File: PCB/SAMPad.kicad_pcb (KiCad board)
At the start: 2 copper layers, 73.2 x 116 mm, 162 parts, among them P1 USB_CONN, P1_2 USB_CONN, P4 CONN_6, P5 CONN_6, P6 ISP6, U1 ATMEGA32U4, U3 IP4234CZ6, U4 AP3417C, U5 PAM2804, X1 CRYSTAL

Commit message: v0.3
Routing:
- net VSS: track 537.2 -> 487.0 mm
- net /mcu/ROW6: track 137.2 -> 134.4 mm, vias 2 -> 4
- net 3V3: track 491.5 -> 494.1 mm

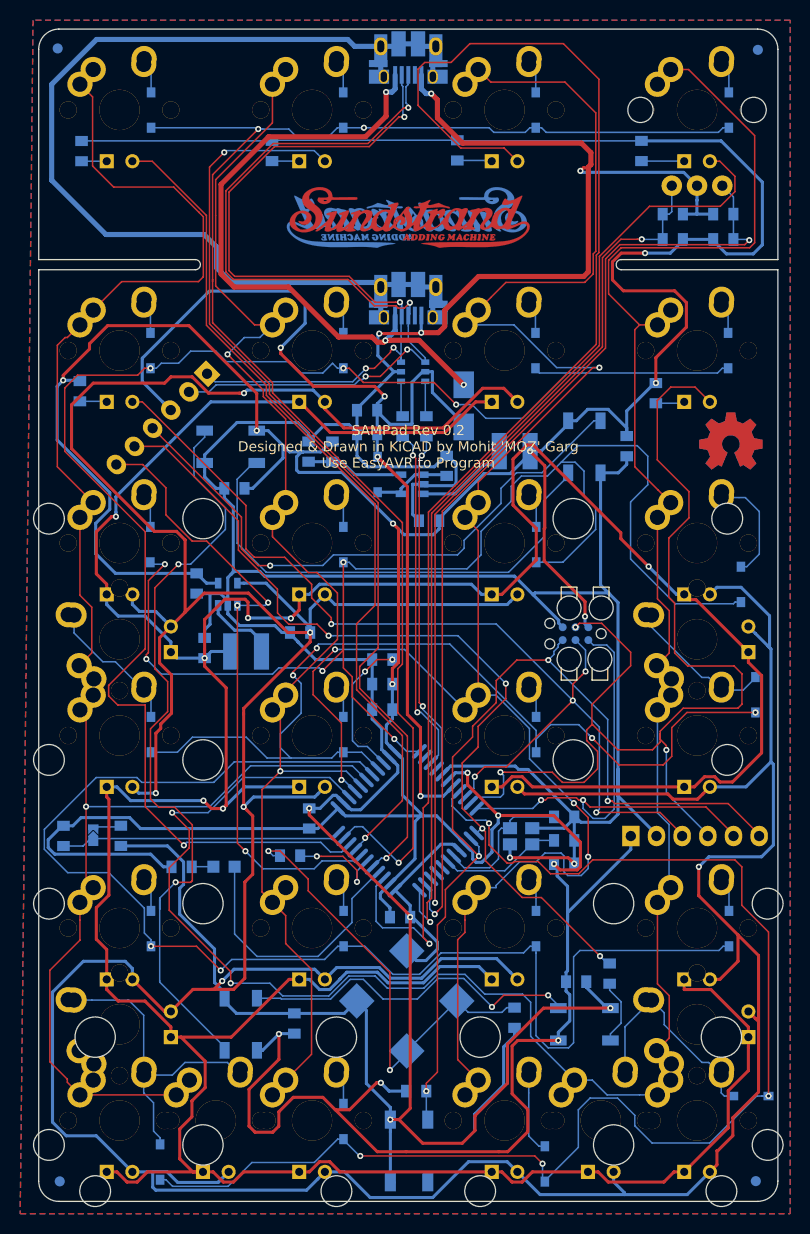
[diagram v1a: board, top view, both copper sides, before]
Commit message: Rev 0.4 - Removed 3.3V regulator
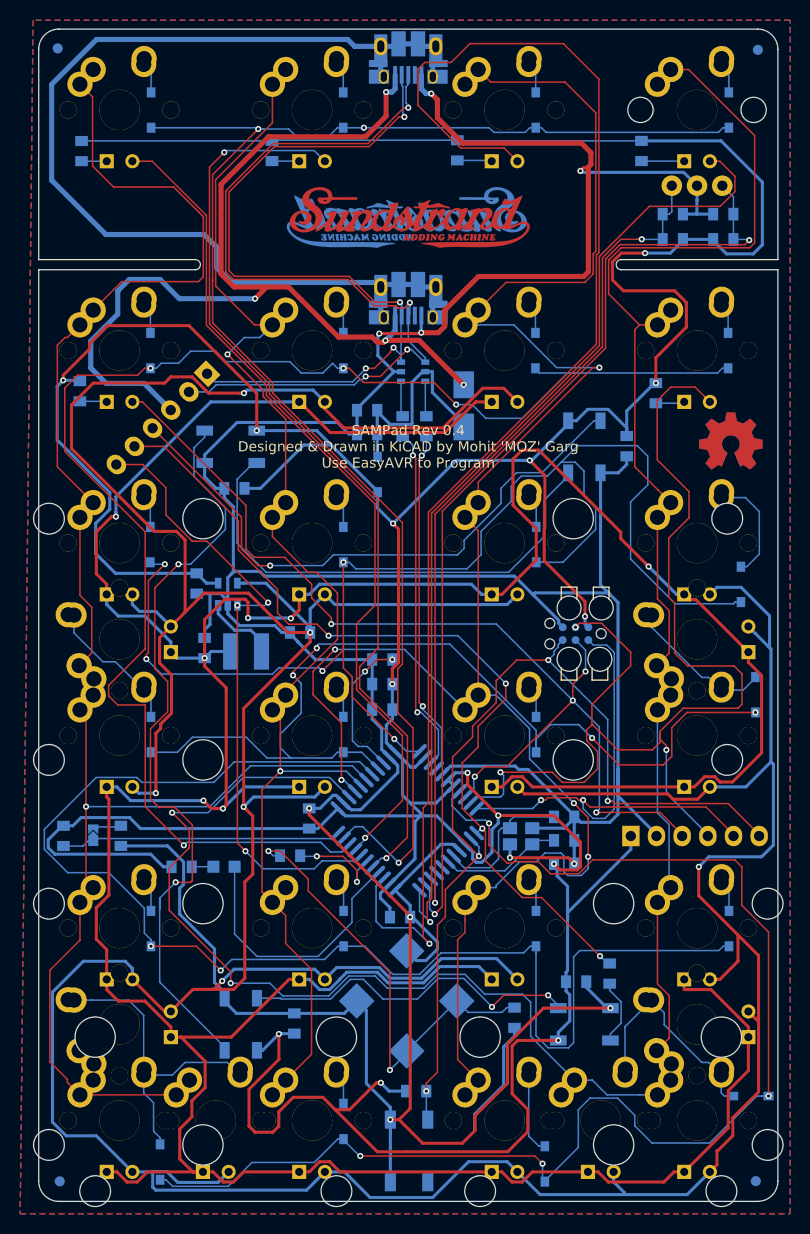
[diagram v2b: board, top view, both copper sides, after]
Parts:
- removed C15: 4.7uF, prettylib:SMD_0805
- removed C16: 10uF, prettylib:SMD_0805
- removed L1: 2.2uH, prettylib:Inductor_Bourn_4mmx4mm
- removed R7: 453k, prettylib:SMD_0805
- removed R8: 100k, prettylib:SMD_0805
- removed U4: AP3417C, prettylib:SOT-23-5
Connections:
- C1 pad 1: /mcu/VUSB -> Net-(C1-Pad1)
- C17 pad 1: 3V3 -> +5V
- C2 pad 1: 3V3 -> +5V
- C3 pad 1: 3V3 -> +5V
- C4 pad 1: 3V3 -> +5V
- C6 pad 1: 3V3 -> +5V
- C7 pad 1: 3V3 -> +5V
- C9 pad 1: /mcu/VUSB -> Net-(C1-Pad1)
- CLED1 pad 2: 3V3 -> +5V
- CLED2 pad 2: 3V3 -> +5V
- CLED3 pad 1: 3V3 -> +5V
- CLED4 pad 1: 3V3 -> +5V
- D1 pad 1: /mcu/VUSB -> Net-(C1-Pad1)
- D1 pad 2: /mcu/VINU -> +5V
- F1 pad 1: Net-(F1-Pad1) -> /mcu/VUSB
- F1 pad 2: /mcu/VUSB -> Net-(C1-Pad1)
- LEDG1 pad 1: 3V3 -> +5V
- LEDG2 pad 1: 3V3 -> +5V
- LEDG3 pad 1: 3V3 -> +5V
- LEDG4 pad 1: 3V3 -> +5V
- P1 pad 1: Net-(F1-Pad1) -> /mcu/VUSB
- P1_2 pad 1: Net-(F1-Pad1) -> /mcu/VUSB
- P5 pad 1: 3V3 -> +5V
- P6 pad 2: 3V3 -> +5V
- R14 pad 2: 3V3 -> +5V
- R34 pad 2: 3V3 -> +5V
- R35 pad 1: 3V3 -> +5V
- R9 pad 2: 3V3 -> +5V
- RI1 pad 2: 3V3 -> +5V
- RI2 pad 2: 3V3 -> +5V
- RI3 pad 2: 3V3 -> +5V
- RI4 pad 2: 3V3 -> +5V
- RI5 pad 2: 3V3 -> +5V
- RI6 pad 2: 3V3 -> +5V
- RI7 pad 2: 3V3 -> +5V
- U1 pad 14: 3V3 -> +5V
- U1 pad 2: (no net) -> +5V
- U1 pad 24: 3V3 -> +5V
- U1 pad 34: 3V3 -> +5V
- U1 pad 44: 3V3 -> +5V
- U1 pad 6: 3V3 -> +5V
- U1 pad 7: /mcu/VUSB -> +5V
- U3 pad 5: /mcu/VUSB -> Net-(C1-Pad1)
- U5 pad 4: 3V3 -> +5V
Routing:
- net +5V: track 0.00 -> 501.0 mm, vias 0 -> 14
- net 3V3: track 494.1 -> 0.00 mm, vias 14 -> 0
- net Net-(F1-Pad1): track 64.4 -> 0.00 mm, vias 3 -> 0
- net VSS: track 487.0 -> 461.3 mm
- net Net-(C1-Pad1): track 0.00 -> 22.1 mm
- net Net-(L1-Pad2): track 9.89 -> 0.00 mm
- net Net-(R7-Pad2): track 9.68 -> 0.00 mm
- net /mcu/VINU: track 8.04 -> 0.00 mm
- net /mcu/VUSB: track 106.5 -> 99.2 mm
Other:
- board text added: "SAMPad Rev 0.4 Designed & Drawin in KiCAD by Mohit 'MOZ' Garg Use EasyAVR to Program"
- board text added: "SAMPad Rev 0.4 Designed & Drawn in KiCAD by Mohit 'MOZ' Garg Use EasyAVR to Program"
- board text removed: "SAMPad Rev 0.2 Designed & Drawin in KiCAD by Mohit 'MOZ' Garg Use EasyAVR to Program"
- board text removed: "SAMPad Rev 0.2 Designed & Drawn in KiCAD by Mohit 'MOZ' Garg Use EasyAVR to Program"

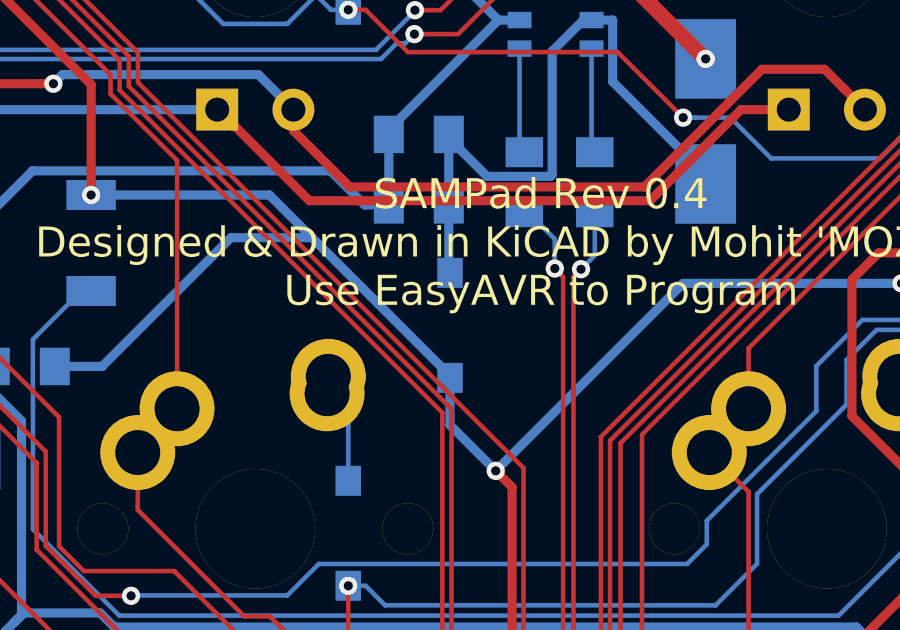
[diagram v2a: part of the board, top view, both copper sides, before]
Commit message: Removed Shottky diode
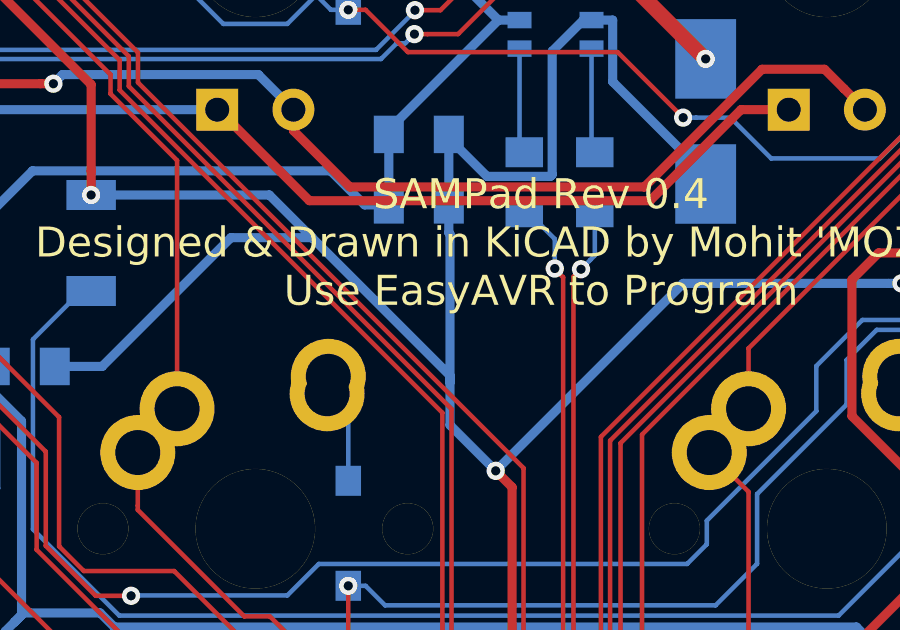
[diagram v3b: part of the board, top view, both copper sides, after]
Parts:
- removed D1: SCHOTTKY, prettylib:SOD123-DIODE
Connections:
- C1 pad 1: Net-(C1-Pad1) -> +5V
- C9 pad 1: Net-(C1-Pad1) -> +5V
- F1 pad 2: Net-(C1-Pad1) -> +5V
- U3 pad 5: Net-(C1-Pad1) -> +5V
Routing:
- net +5V: track 501.0 -> 526.7 mm
- net Net-(C1-Pad1): track 22.1 -> 0.00 mm
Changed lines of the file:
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@@
 (kicad_pcb (version 4) (host pcbnew 4.0.1-stable)
   (general
-    (links 366)
-    (no_connects 1)
+    (links 365)
+    (no_connects 0)
     (area 91.936499 68.123999 165.213501 184.263501)
     (thickness 1.6)
     (drawings 21)
-    (tracks 2026)
+    (tracks 2028)
     (zones 0)
-    (modules 156)
-    (nets 81)
+    (modules 155)
+    (nets 80)
   )
   (page A4)
@@
   )
   (setup
-    (last_trace_width 0.508)
+    (last_trace_width 0.1524)
     (user_trace_width 0.1524)
     (user_trace_width 0.2032)
@@
   (net 78 "Net-(BZ1-Pad1)")
   (net 79 +5V)
-  (net 80 "Net-(C1-Pad1)")
   (net_class Default "This is the default net class."
     (clearance 0.1524)
@@
     (add_net /mcu/XTAL2)
     (add_net "Net-(BZ1-Pad1)")
-    (add_net "Net-(C1-Pad1)")
     (add_net "Net-(C5-Pad1)")
     (add_net "Net-(D1:1-Pad1)")
@@
       (net 63 /mcu/D+))
     (pad 5 smd rect (at 0 1.2 90) (size 0.55 0.8) (layers B.Cu B.Paste B.Mask)
-      (net 80 "Net-(C1-Pad1)"))
+      (net 79 +5V))
     (pad 6 smd rect (at -0.95 1.2 90) (size 0.55 0.8) (layers B.Cu B.Paste B.Mask)
       (net 69 "Net-(R3-Pad1)"))
@@
       (net 2 /mcu/VUSB))
     (pad 2 smd rect (at 2.08534 0 180) (size 2.02946 2.65176) (layers B.Cu B.Paste B.Mask)
-      (net 80 "Net-(C1-Pad1)"))
+      (net 79 +5V))
   )
   (module prettylib:SOD123-DIODE (layer B.Cu)
@@
     )
   )
-  (module prettylib:SOD123-DIODE (layer B.Cu)
-    (at 125.5395 112.268)
-    (descr DIODE)
-    (tags DIODE)
-    (fp_text reference D1 (at -1.7145 0.127 270) (layer B.SilkS)
-      (effects (font (size 1.016 1.016) (thickness 0.2032)) (justify mirror))
-    )
-    (fp_text value SCHOTTKY (at 1.905 0 270) (layer B.SilkS) hide
-      (effects (font (size 1.016 1.016) (thickness 0.2032)) (justify mirror))
-    )
-    (fp_line (start -0.8509 0.70104) (end 0.8509 0.70104) (layer B.SilkS) (width 0.22098))
-    (fp_line (start -0.8509 1.45034) (end -0.59944 1.45034) (layer B.SilkS) (width 0.22098))
-    (fp_line (start 0.8509 1.45034) (end 0.59944 1.45034) (layer B.SilkS) (width 0.22098))
-    (fp_line (start 0.8509 -1.45034) (end 0.59944 -1.45034) (layer B.SilkS) (width 0.22098))
-    (fp_line (start -0.8509 -1.45034) (end -0.59944 -1.45034) (layer B.SilkS) (width 0.22098))
-    (fp_line (start -0.8509 -1.45034) (end -0.8509 1.45034) (layer B.SilkS) (width 0.22098))
-    (fp_line (start 0.8509 -1.45034) (end 0.8509 1.45034) (layer B.SilkS) (width 0.22098))
-    (pad 2 smd rect (at 0 1.7526 90) (size 1.00076 0.8509) (layers B.Cu B.Paste B.Mask)
-      (net 79 +5V))
-    (pad 1 smd rect (at 0 -1.74752 90) (size 1.00076 0.8509) (layers B.Cu B.Paste B.Mask)
-      (net 80 "Net-(C1-Pad1)"))
-    (model SOD123.wrl
-      (at (xyz 0 0 -0.003))
-      (scale (xyz 0.393701 0.393701 0.393701))
-      (rotate (xyz 0 0 90))
-    )
-  )
   (module prettylib:SMD_0805 (layer B.Cu)
     (at 150.1902 109.4613 270)
@@
     (fp_line (start 1.8 1) (end 1.8 -1) (layer B.SilkS) (width 0.15))
     (pad 1 smd rect (at -1 0 180) (size 1 1.25) (layers B.Cu B.Paste B.Mask)
-      (net 80 "Net-(C1-Pad1)"))
+      (net 79 +5V))
     (pad 2 smd rect (at 1 0 180) (size 1 1.25) (layers B.Cu B.Paste B.Mask)
       (net 1 VSS))
@@
     (fp_line (start 1.8 1) (end 1.8 -1) (layer B.SilkS) (width 0.15))
     (pad 1 smd rect (at -1 0 180) (size 1 1.25) (layers B.Cu B.Paste B.Mask)
-      (net 80 "Net-(C1-Pad1)"))
+      (net 79 +5V))
     (pad 2 smd rect (at 1 0 180) (size 1 1.25) (layers B.Cu B.Paste B.Mask)
       (net 1 VSS))
@@
   (segment (start 128.4224 169.313147) (end 129.376993 168.358554) (width 0.1524) (layer B.Cu) (net 78))
   (segment (start 129.376993 168.358554) (end 133.372147 164.3634) (width 0.1524) (layer B.Cu) (net 78))
+  (segment (start 125.5395 114.0206) (end 125.5395 114.173) (width 0.3048) (layer B.Cu) (net 79))
+  (segment (start 125.5395 114.173) (end 125.5395 115.5954) (width 0.3048) (layer B.Cu) (net 79))
+  (segment (start 125.5 108.2548) (end 125.5 109.1846) (width 0.3048) (layer B.Cu) (net 79))
+  (segment (start 125.5 109.1846) (end 125.5395 109.2241) (width 0.3048) (layer B.Cu) (net 79))
+  (segment (start 125.5395 109.2241) (end 125.5395 114.173) (width 0.3048) (layer B.Cu) (net 79))
   (segment (start 133.080071 143.057241) (end 133.040759 143.057241) (width 0.3048) (layer B.Cu) (net 79))
   (segment (start 133.040759 143.057241) (end 131.318 144.78) (width 0.3048) (layer B.Cu) (net 79))
@@
   (segment (start 144.4 106.948) (end 144.4 107.2735) (width 0.3048) (layer B.Cu) (net 79))
   (segment (start 140.157948 110.871) (end 140.589 110.871) (width 0.3048) (layer B.Cu) (net 79))
-  (segment (start 125.5395 114.0206) (end 125.5395 115.5954) (width 0.3048) (layer B.Cu) (net 79))
   (segment (start 125.5395 115.5954) (end 127.0635 117.1194) (width 0.3048) (layer B.Cu) (net 79))
   (segment (start 125.505454 179.2859) (end 121.352554 175.133) (width 0.3048) (layer F.Cu) (net 79))
@@
   (segment (start 151.6507 79.2513) (end 133.4897 79.2513) (width 0.1524) (layer B.Cu) (net 79))
   (segment (start 133.4897 79.2513) (end 133.4262 79.1878) (width 0.1524) (layer B.Cu) (net 79))
-  (segment (start 125.5 108.2548) (end 125.5 110.48098) (width 0.3048) (layer B.Cu) (net 80))
-  (segment (start 125.5 110.48098) (end 125.5395 110.52048) (width 0.3048) (layer B.Cu) (net 80))
-  (segment (start 125.5 105.9053) (end 125.5 108.2548) (width 0.3048) (layer B.Cu) (net 80))
-  (segment (start 130.2574 102.0953) (end 129.983758 102.0953) (width 0.3048) (layer B.Cu) (net 80))
-  (segment (start 128.945801 103.133257) (end 128.945801 107.243841) (width 0.3048) (layer B.Cu) (net 80))
-  (segment (start 129.983758 102.0953) (end 128.945801 103.133257) (width 0.3048) (layer B.Cu) (net 80))
-  (segment (start 128.945801 107.243841) (end 128.884841 107.304801) (width 0.3048) (layer B.Cu) (net 80))
-  (segment (start 128.884841 107.304801) (end 126.774501 107.304801) (width 0.3048) (layer B.Cu) (net 80))
-  (segment (start 126.774501 107.304801) (end 125.5 106.0303) (width 0.3048) (layer B.Cu) (net 80))
-  (segment (start 125.5 106.0303) (end 125.5 105.9053) (width 0.3048) (layer B.Cu) (net 80))
-  (segment (start 134.0612 107.55884) (end 134.0612 107.24769) (width 0.3048) (layer B.Cu) (net 80))
-  (segment (start 134.0612 107.24769) (end 130.962201 104.148691) (width 0.3048) (layer B.Cu) (net 80))
-  (segment (start 130.962201 104.148691) (end 130.9622 102.0953) (width 0.3048) (layer B.Cu) (net 80))
-  (segment (start 130.9622 102.0953) (end 130.2574 102.0953) (width 0.3048) (layer B.Cu) (net 80))
+  (segment (start 125.5 105.9053) (end 125.5 108.2548) (width 0.3048) (layer B.Cu) (net 79))
+  (segment (start 130.2574 102.0953) (end 129.983758 102.0953) (width 0.3048) (layer B.Cu) (net 79))
+  (segment (start 128.945801 103.133257) (end 128.945801 107.243841) (width 0.3048) (layer B.Cu) (net 79))
+  (segment (start 129.983758 102.0953) (end 128.945801 103.133257) (width 0.3048) (layer B.Cu) (net 79))
+  (segment (start 128.945801 107.243841) (end 128.884841 107.304801) (width 0.3048) (layer B.Cu) (net 79))
+  (segment (start 128.884841 107.304801) (end 126.774501 107.304801) (width 0.3048) (layer B.Cu) (net 79))
+  (segment (start 126.774501 107.304801) (end 125.5 106.0303) (width 0.3048) (layer B.Cu) (net 79))
+  (segment (start 125.5 106.0303) (end 125.5 105.9053) (width 0.3048) (layer B.Cu) (net 79))
+  (segment (start 134.0612 107.55884) (end 134.0612 107.24769) (width 0.3048) (layer B.Cu) (net 79))
+  (segment (start 134.0612 107.24769) (end 130.962201 104.148691) (width 0.3048) (layer B.Cu) (net 79))
+  (segment (start 130.962201 104.148691) (end 130.9622 102.0953) (width 0.3048) (layer B.Cu) (net 79))
+  (segment (start 130.9622 102.0953) (end 130.2574 102.0953) (width 0.3048) (layer B.Cu) (net 79))
   (zone (net 0) (net_name "") (layer B.Cu) (hatch edge 0.508)
     (connect_pads (clearance 0.508))

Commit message: Rev 0.5
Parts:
- moved STAB6 4.00 mm to (157.2, 128.6)
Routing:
- net /ledmatrix/LEDI2: track 112.3 -> 108.7 mm
- net Net-(D3:4-Pad1): track 10.9 -> 7.99 mm
- net /mcu/MISO: track 50.8 -> 53.5 mm
- net /ledmatrix/LEDCATH: track 469.3 -> 470.7 mm
- net /mcu/ROW3: track 134.1 -> 132.7 mm
- net VSS: track 461.3 -> 462.5 mm
- net /mcu/ROW4: track 95.0 -> 94.1 mm
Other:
- board text added: "SAMPad Rev 0.5 Designed & Drawin in KiCAD by Mohit 'MOZ' Garg Use EasyAVR to Program"
- board text added: "SAMPad Rev 0.5 Designed & Drawn in KiCAD by Mohit 'MOZ' Garg Use EasyAVR to Program"
- board text removed: "SAMPad Rev 0.4 Designed & Drawin in KiCAD by Mohit 'MOZ' Garg Use EasyAVR to Program"
- board text removed: "SAMPad Rev 0.4 Designed & Drawn in KiCAD by Mohit 'MOZ' Garg Use EasyAVR to Program"

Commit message: Minor update to correct silkscreen on Rev 0.5
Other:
- rule pad_to_mask_clearance: 0.2032 -> 0.1016

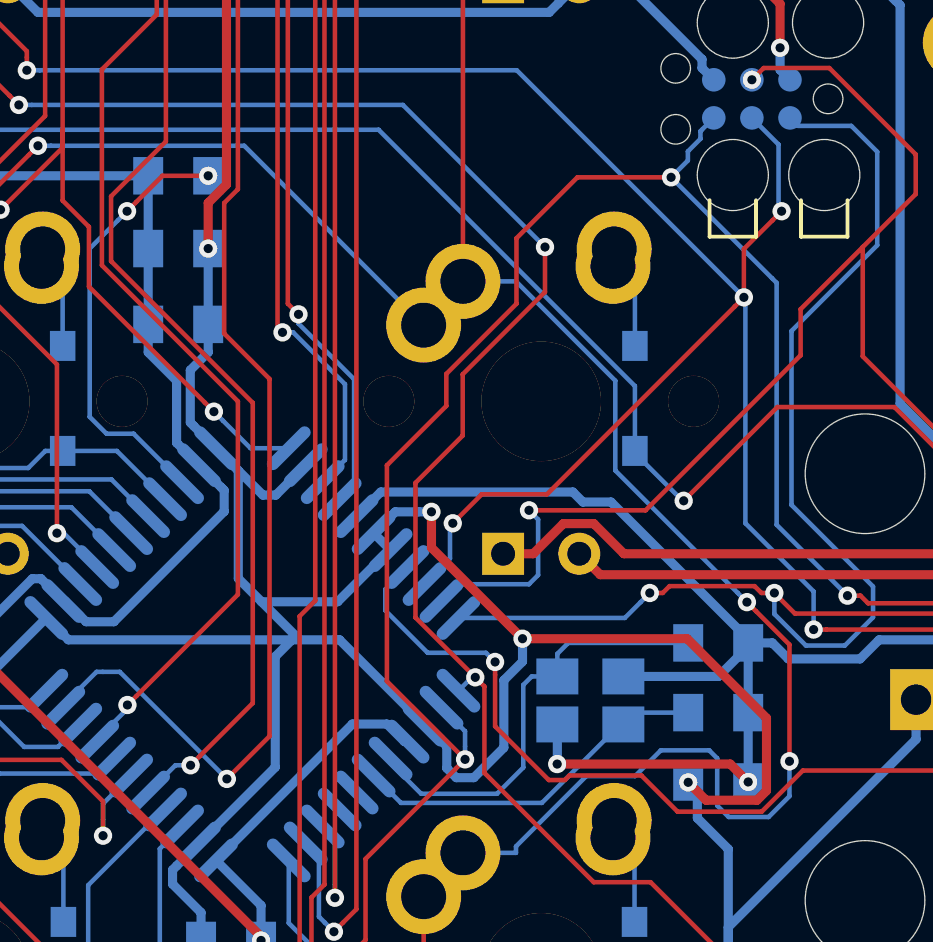
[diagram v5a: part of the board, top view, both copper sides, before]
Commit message: Minor revision update, corrected the UCAP connection on MCU
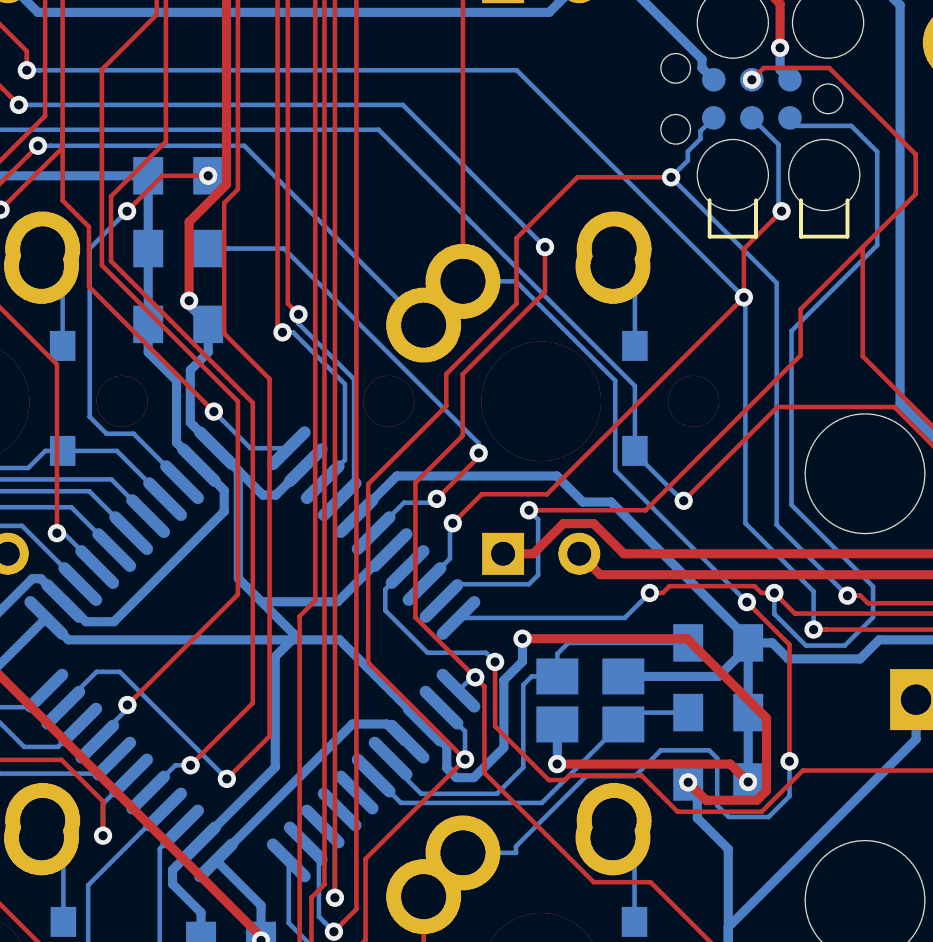
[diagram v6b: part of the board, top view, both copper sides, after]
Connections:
- C2 pad 1: +5V -> Net-(C2-Pad1)
- U1 pad 6: +5V -> Net-(C2-Pad1)
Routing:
- net Net-(C2-Pad1): track 0.00 -> 16.9 mm, vias 0 -> 2
- net +5V: track 526.7 -> 518.6 mm, vias 14 -> 13
- net /mcu/MCURST: track 92.0 -> 92.6 mm
